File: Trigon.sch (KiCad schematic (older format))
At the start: 1 part

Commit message: Fully laid out board
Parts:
- removed U?: ProMicro, symbol keebio:ProMicro
- added D1, D10, D11, D12, D13, D14, D15, D16, D17, D18, D19, D2, D20, D21, D22, D23, D24, D25, D3, D4, D5, D6, D7, D8, D9: D_Small, Keebio-Parts:Diode, symbol Device:D_Small
- added MX1, MX10, MX11, MX12, MX13, MX14, MX15, MX16, MX17, MX18, MX19, MX2, MX20, MX21, MX22, MX23, MX24, MX25, MX3, MX4, MX5, MX6, MX7, MX8, MX9: MX-NoLED, MX_Alps_Hybrid:MX-1U-NoLED, symbol MX_Alps_Hybrid:MX-NoLED
- added U1: ProMicro, Keebio-Parts:ArduinoProMicro-ZigZag, symbol keebio:ProMicro
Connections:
- new net: D1.2 (A), MX1.2 (ROW)
- new net: D2.2 (A), MX2.2 (ROW)
- new net: D3.2 (A), MX3.2 (ROW)
- new net: D4.2 (A), MX4.2 (ROW)
- new net: D5.2 (A), MX5.2 (ROW)
- new net: D6.2 (A), MX6.2 (ROW)
- new net: D7.2 (A), MX7.2 (ROW)
- new net: D8.2 (A), MX8.2 (ROW)
- new net: D9.2 (A), MX9.2 (ROW)
- new net: D10.2 (A), MX10.2 (ROW)
- new net: D11.2 (A), MX11.2 (ROW)
- new net: D12.2 (A), MX12.2 (ROW)
- new net: D13.2 (A), MX13.2 (ROW)
- new net: D14.2 (A), MX14.2 (ROW)
- new net: D15.2 (A), MX15.2 (ROW)
- new net: D16.2 (A), MX16.2 (ROW)
- new net: D17.2 (A), MX17.2 (ROW)
- new net: D18.2 (A), MX18.2 (ROW)
- new net: D19.2 (A), MX19.2 (ROW)
- new net: D20.2 (A), MX20.2 (ROW)
- new net: D21.2 (A), MX21.2 (ROW)
- new net: D22.2 (A), MX22.2 (ROW)
- new net: D23.2 (A), MX23.2 (ROW)
- new net: D24.2 (A), MX24.2 (ROW)
- new net: D25.2 (A), MX25.2 (ROW)
- new net COL0: MX1.1 (COL), MX14.1 (COL), MX19.1 (COL), MX23.1 (COL), MX8.1 (COL), U1.8 (5/PC6)
- new net COL1: MX15.1 (COL), MX2.1 (COL), MX20.1 (COL), MX24.1 (COL), MX9.1 (COL), U1.7 (4/PD4)
- new net COL2: MX10.1 (COL), MX16.1 (COL), MX21.1 (COL), MX25.1 (COL), MX3.1 (COL), U1.6 (3/PD0)
- new net COL3: MX11.1 (COL), MX17.1 (COL), MX22.1 (COL), MX4.1 (COL), U1.5 (2/PD1)
- new net COL4: MX12.1 (COL), MX18.1 (COL), MX5.1 (COL), U1.9 (6/PD7)
- new net COL5: MX13.1 (COL), MX6.1 (COL), U1.10 (7/PE6)
- new net COL6: MX7.1 (COL), U1.11 (8/PB4)
- new net ROW0: D1.1 (K), D2.1 (K), D3.1 (K), D4.1 (K), D5.1 (K), D6.1 (K), D7.1 (K), U1.16 (15/PB1)
- new net ROW1: D10.1 (K), D11.1 (K), D12.1 (K), D13.1 (K), D8.1 (K), D9.1 (K), U1.17 (A0/PF7)
- new net ROW2: D14.1 (K), D15.1 (K), D16.1 (K), D17.1 (K), D18.1 (K), U1.18 (A1/PF6)
- new net ROW3: D19.1 (K), D20.1 (K), D21.1 (K), D22.1 (K), U1.19 (A2/PF5)
- new net ROW4: D23.1 (K), D24.1 (K), D25.1 (K), U1.20 (A3/PF4)

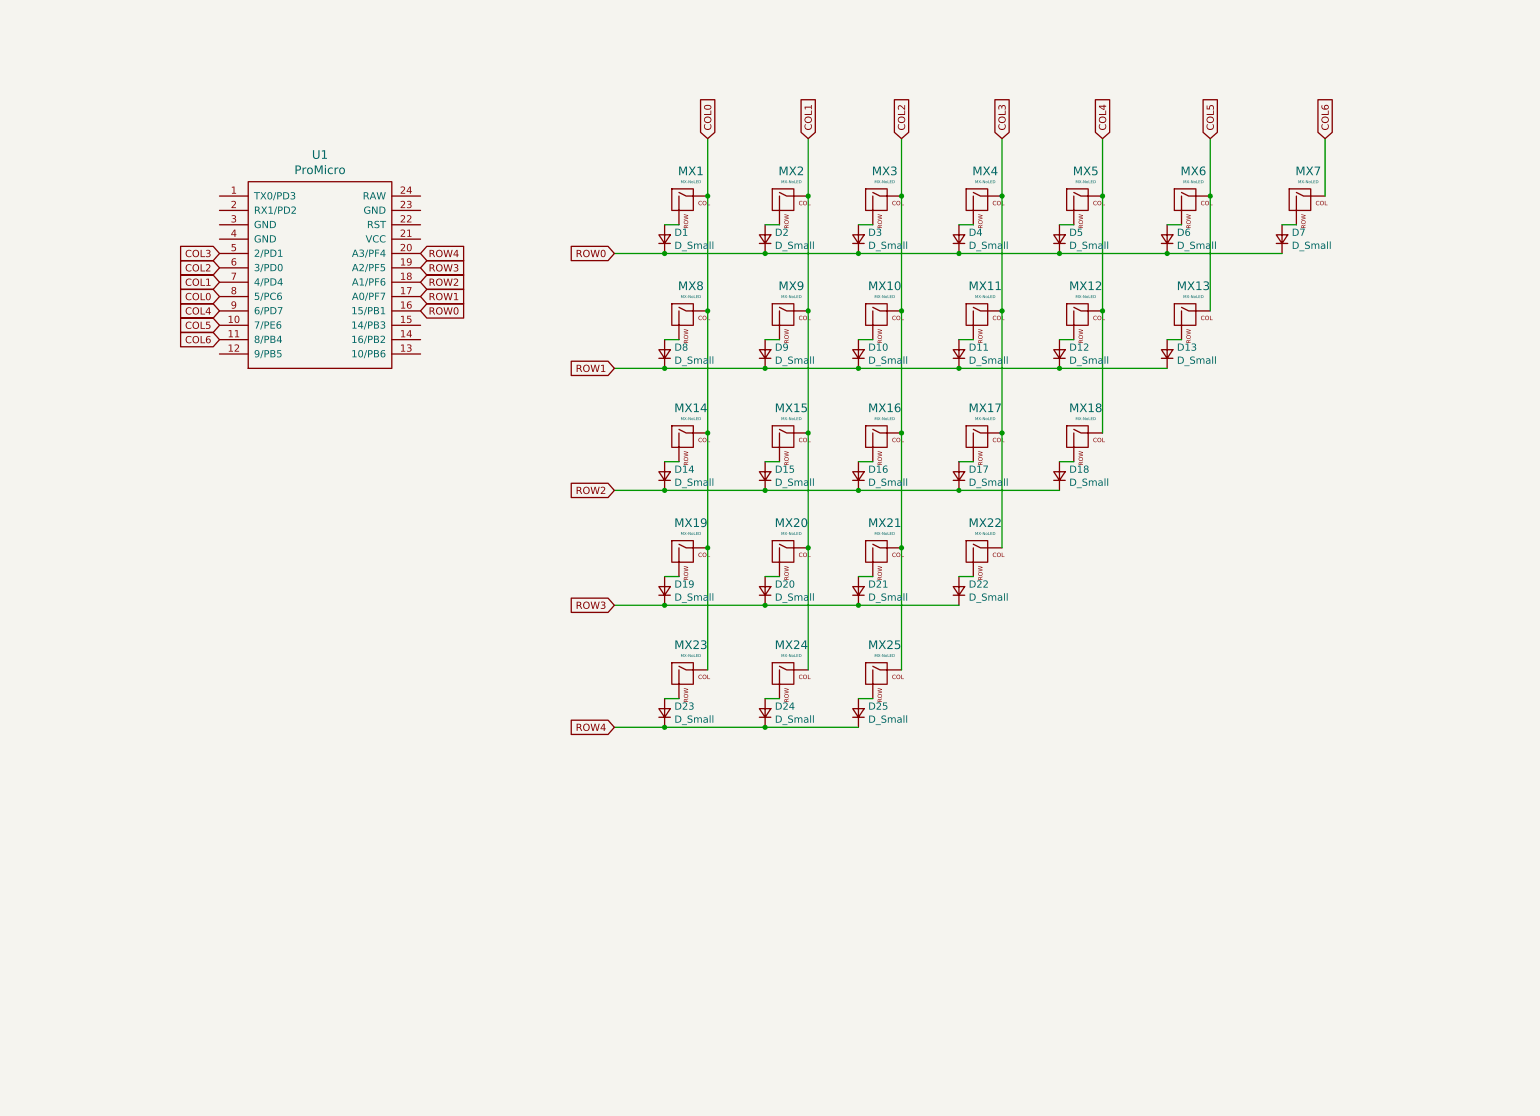
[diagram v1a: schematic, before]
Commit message: onboard usb c
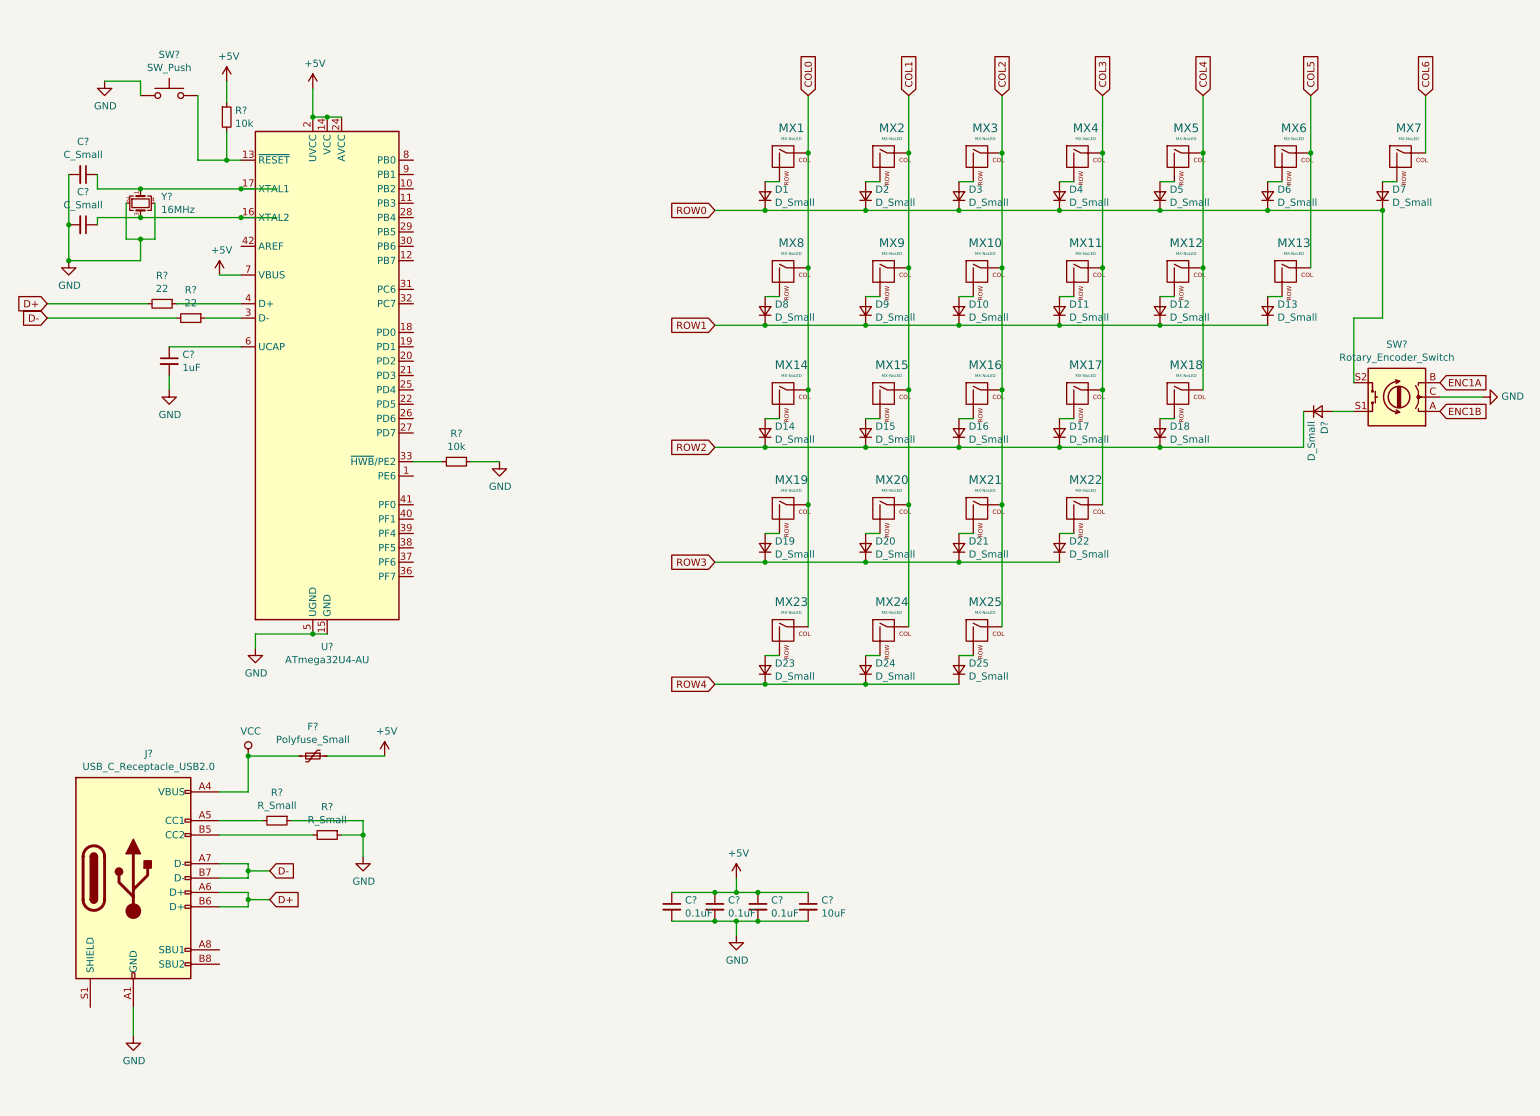
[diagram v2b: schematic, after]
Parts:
- removed U1: ProMicro, Keebio-Parts:ArduinoProMicro-ZigZag, symbol keebio:ProMicro
- added C?: 1uF, symbol Device:C_Small
- added C? (x3): 0.1uF, symbol Device:C_Small
- added C?: 10uF, symbol Device:C_Small
- added C? (x2): C_Small, symbol Device:C_Small
- added D?: D_Small, Keebio-Parts:Diode, symbol Device:D_Small
- added F?: Polyfuse_Small, symbol Device:Polyfuse_Small
- added J?: USB_C_Receptacle_USB2.0, symbol Connector:USB_C_Receptacle_USB2.0
- added R? (x2): 10k, symbol Device:R_Small
- added R? (x2): 22, symbol Device:R_Small
- added R? (x2): R_Small, symbol Device:R_Small
- added SW?: Rotary_Encoder_Switch, symbol Device:Rotary_Encoder_Switch
- added SW?: SW_Push, symbol Switch:SW_Push
- added U?: ATmega32U4-AU, Package_QFP:TQFP-44_10x10mm_P0.8mm, symbol MCU_Microchip_ATmega:ATmega32U4-AU
- added Y?: 16MHz, symbol Device:Crystal_GND24_Small
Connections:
- net ROW0: now also SW?.S2
- net ROW2: now also D?.1 (K)
- new net: R?.2, SW?.2, U?.13 (~RESET)
- new net: C?.1, U?.16 (XTAL2), Y?.3
- new net: C?.1, U?.17 (XTAL1), Y?.1
- new net: R?.1, U?.3 (D-)
- new net: R?.2, U?.33 (~HWB~/PE2)
- new net: R?.1, U?.4 (D+)
- new net: C?.1, U?.6 (UCAP)
- new net: D?.2 (A), SW?.S1
- new net: J?.A5 (CC1), R?.2
- new net: J?.B5 (CC2), R?.2
- new net +5V: C?.1, C?.1, C?.1, C?.1, F?.1, R?.1, U?.14 (VCC), U?.2 (UVCC), U?.24 (AVCC), U?.34 (VCC), U?.44 (AVCC), U?.7 (VBUS)
- new net D+: J?.A6 (D+), J?.B6 (D+), R?.2
- new net D-: J?.A7 (D-), J?.B7 (D-), R?.2
- new net ENC1A: SW?.B
- new net ENC1B: SW?.A
- new net GND: C?.2, C?.2, C?.2, C?.2, C?.2, C?.2, C?.2, J?.A1 (GND), J?.A12 (GND), J?.B1 (GND), J?.B12 (GND), R?.1, R?.1, R?.1, SW?.1, SW?.C, U?.15 (GND), U?.23 (GND), U?.35 (GND), U?.43 (GND), U?.5 (UGND), Y?.2, Y?.4
- new net VCC: F?.2, J?.A4 (VBUS), J?.A9 (VBUS), J?.B4 (VBUS), J?.B9 (VBUS)
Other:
- moved on the sheet: D1, D10, D11, D12, D13, D14, D15, D16, D17, D18, D19, D2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

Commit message: routed without rows cols
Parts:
- C1, C2: renamed from C?; value C_Small -> 22pF; footprint (none) -> Capacitor_SMD:C_0805_2012Metric
- C3, C4, C5, C6: renamed from C?; footprint (none) -> Capacitor_SMD:C_0805_2012Metric
- C7: renamed from C?; footprint (none) -> Diode_SMD:D_SOD-123
- D1, D10, D11, D12, D13, D14, D15, D16, D17, D18, D19, D2, D20, D21, D22, D23, D24, D25, D3, D4, D5, D6, D7, D8, D9: footprint Keebio-Parts:Diode -> Diode_SMD:D_SOD-123
- D26: renamed from D?; footprint Keebio-Parts:Diode -> Diode_SMD:D_SOD-123
- F1: renamed from F?; footprint (none) -> Fuse:Fuse_1206_3216Metric
- J1: renamed from J?; footprint (none) -> Connector_USB:USB_C_Receptacle_Palconn_UTC16-G
- MX1, MX10, MX11, MX12, MX13, MX14, MX15, MX16, MX17, MX18, MX19, MX2, MX20, MX21, MX22, MX23, MX24, MX25, MX3, MX4, MX5, MX6, MX7, MX8, MX9: footprint MX_Alps_Hybrid:MX-1U-NoLED -> MX_Only:MXOnly-1U-NoLED
- R1, R2, R3, R4, R5, R6: renamed from R?; footprint (none) -> Resistor_SMD:R_0805_2012Metric
- SW1: renamed from SW?; footprint (none) -> random-keyboard-parts:SKQG-1155865
- SW2: renamed from SW?; footprint (none) -> Rotary_Encoder:RotaryEncoder_Alps_EC12E-Switch_Vertical_H20mm
- Y1: renamed from Y?; footprint (none) -> Crystal:Crystal_SMD_3225-4Pin_3.2x2.5mm
- gave numbers to parts that had none: 1
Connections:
- net COL5: now also SW2.S2
- net GND: now also J1.S1 (SHIELD)
- net ROW0: no longer SW2.S2

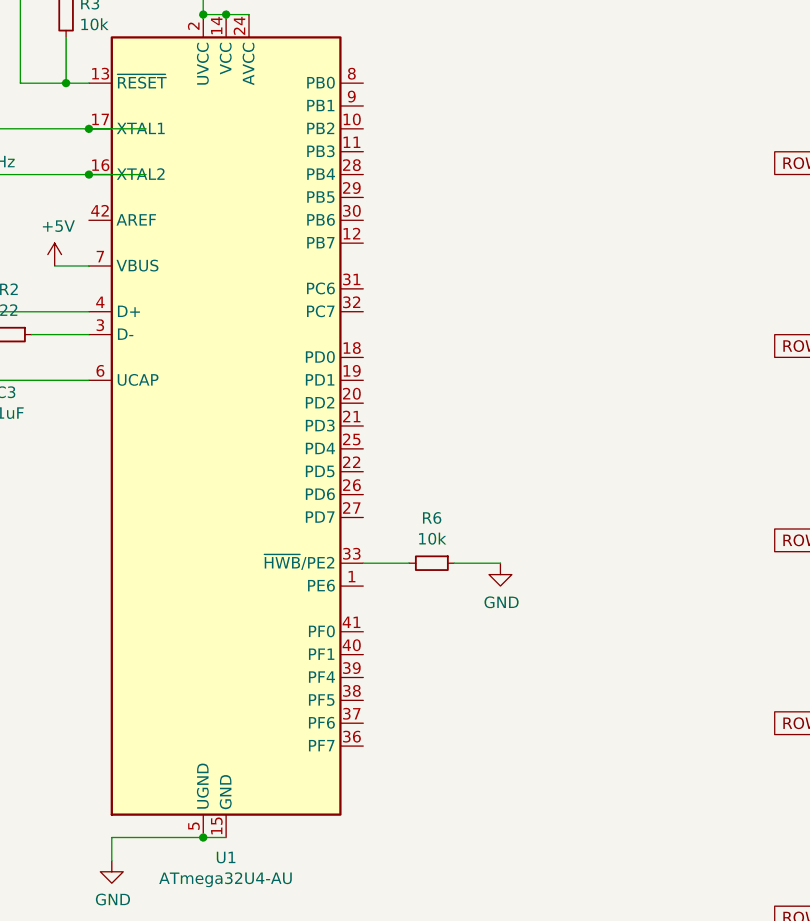
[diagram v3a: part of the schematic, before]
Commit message: fully routed matrix
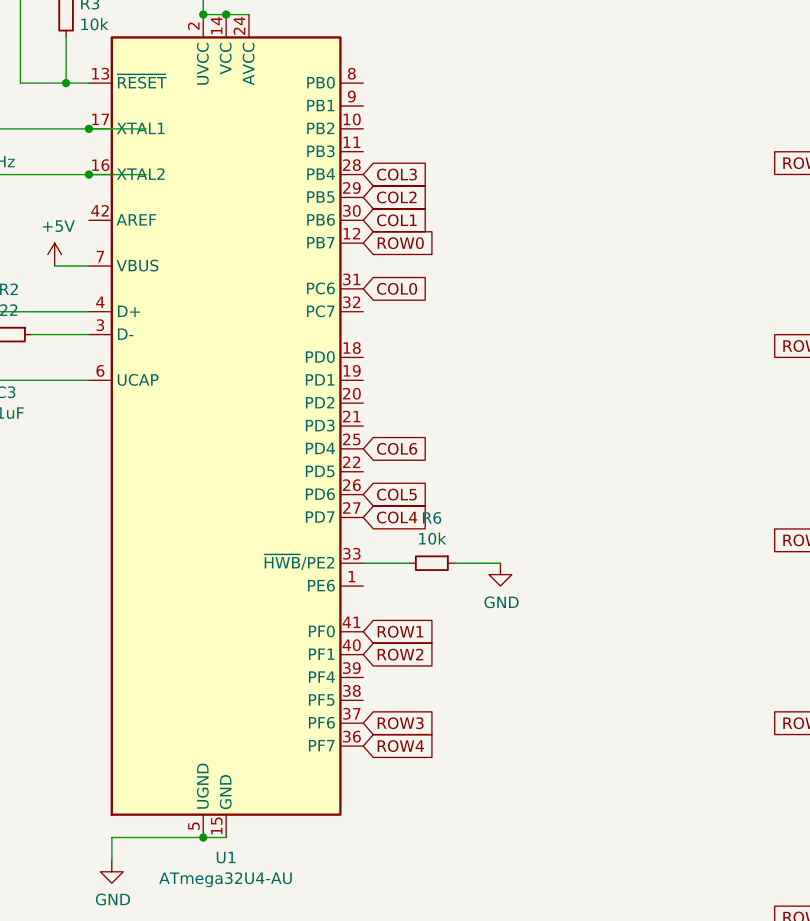
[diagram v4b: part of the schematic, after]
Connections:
- net COL0: now also U1.31 (PC6)
- net COL1: now also U1.30 (PB6)
- net COL2: now also U1.29 (PB5)
- net COL3: now also U1.28 (PB4)
- net COL4: now also U1.27 (PD7)
- net COL5: now also U1.26 (PD6)
- net COL6: now also U1.25 (PD4)
- net ROW0: now also U1.12 (PB7)
- net ROW1: now also U1.41 (PF0)
- net ROW2: now also U1.40 (PF1)
- net ROW3: now also U1.37 (PF6)
- net ROW4: now also U1.36 (PF7)
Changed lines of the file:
@@
 	9500 2950 9500 2150
 Connection ~ 9500 2150
+Text GLabel 3250 2300 2    50   Input ~ 0
+COL0
+Text GLabel 3250 2000 2    50   Input ~ 0
+COL1
+Text GLabel 3250 1900 2    50   Input ~ 0
+COL2
+Text GLabel 3250 1800 2    50   Input ~ 0
+COL3
+Text GLabel 3250 3300 2    50   Input ~ 0
+COL4
+Text GLabel 3250 3200 2    50   Input ~ 0
+COL5
+Text GLabel 3250 3000 2    50   Input ~ 0
+COL6
+Text GLabel 3250 2100 2    50   Input ~ 0
+ROW0
+Text GLabel 3250 4300 2    50   Input ~ 0
+ROW4
+Text GLabel 3250 4200 2    50   Input ~ 0
+ROW3
+Text GLabel 3250 3900 2    50   Input ~ 0
+ROW2
+Text GLabel 3250 3800 2    50   Input ~ 0
+ROW1
 $EndSCHEMATC

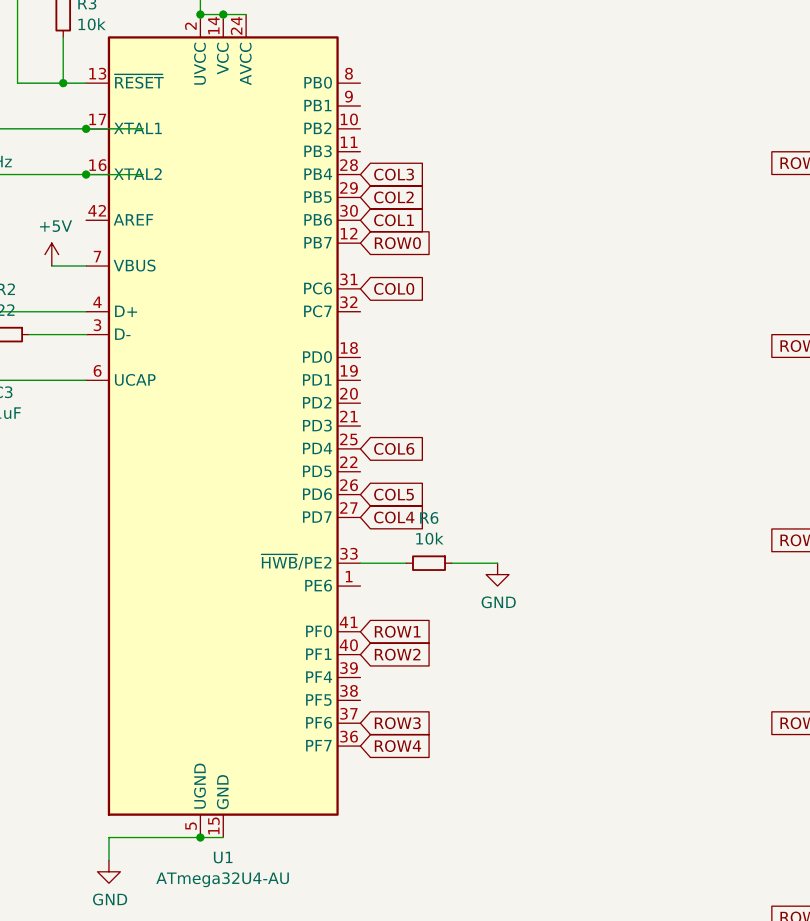
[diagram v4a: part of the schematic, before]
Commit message: all on one side
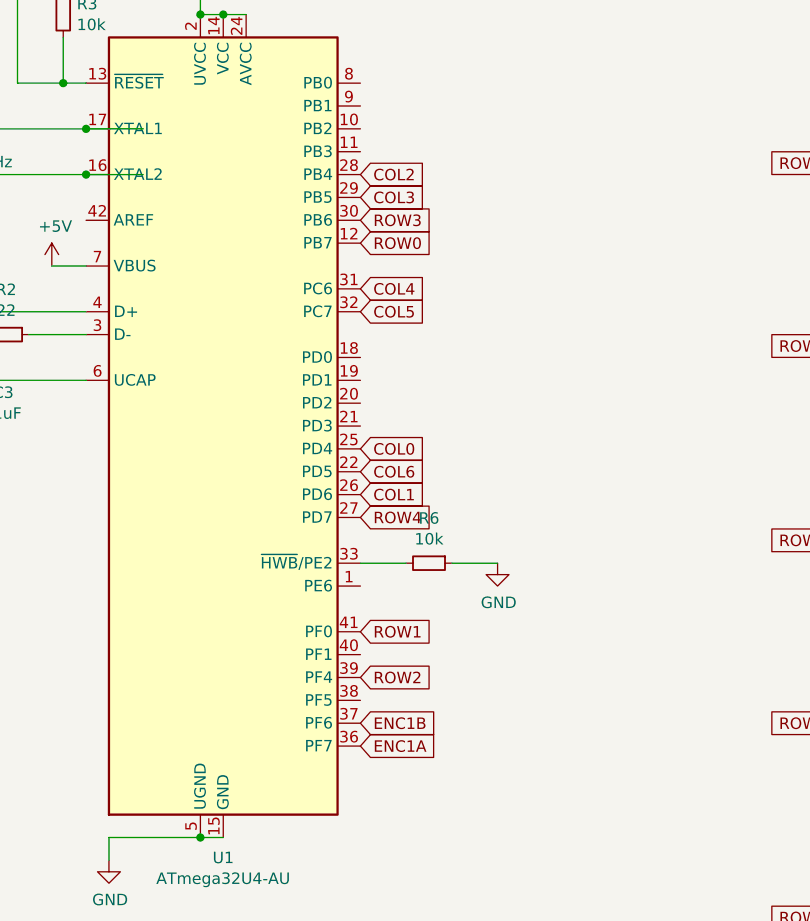
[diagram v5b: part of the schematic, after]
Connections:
- net COL0: now also U1.25 (PD4); no longer U1.31 (PC6)
- net COL1: now also U1.26 (PD6); no longer U1.30 (PB6)
- net COL2: now also U1.28 (PB4); no longer U1.29 (PB5)
- net COL3: now also U1.29 (PB5); no longer U1.28 (PB4)
- net COL4: now also U1.31 (PC6); no longer U1.27 (PD7)
- net COL5: now also U1.32 (PC7); no longer U1.26 (PD6)
- net COL6: now also U1.22 (PD5); no longer U1.25 (PD4)
- net ENC1A: now also U1.36 (PF7)
- net ENC1B: now also U1.37 (PF6)
- net ROW2: now also U1.39 (PF4); no longer U1.40 (PF1)
- net ROW3: now also U1.30 (PB6); no longer U1.37 (PF6)
- net ROW4: now also U1.27 (PD7); no longer U1.36 (PF7)
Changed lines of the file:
@@
 	9500 2950 9500 2150
 Connection ~ 9500 2150
+Text GLabel 3250 3000 2    50   Input ~ 0
+COL0
+Text GLabel 3250 3200 2    50   Input ~ 0
+COL1
+Text GLabel 3250 1800 2    50   Input ~ 0
+COL2
+Text GLabel 3250 1900 2    50   Input ~ 0
+COL3
 Text GLabel 3250 2300 2    50   Input ~ 0
-COL0
-Text GLabel 3250 2000 2    50   Input ~ 0
-COL1
-Text GLabel 3250 1900 2    50   Input ~ 0
-COL2
-Text GLabel 3250 1800 2    50   Input ~ 0
-COL3
-Text GLabel 3250 3300 2    50   Input ~ 0
 COL4
-Text GLabel 3250 3200 2    50   Input ~ 0
+Text GLabel 3250 2400 2    50   Input ~ 0
 COL5
-Text GLabel 3250 3000 2    50   Input ~ 0
+Text GLabel 3250 3100 2    50   Input ~ 0
 COL6
 Text GLabel 3250 2100 2    50   Input ~ 0
 ROW0
-Text GLabel 3250 4300 2    50   Input ~ 0
+Text GLabel 3250 3300 2    50   Input ~ 0
 ROW4
-Text GLabel 3250 4200 2    50   Input ~ 0
+Text GLabel 3250 2000 2    50   Input ~ 0
 ROW3
-Text GLabel 3250 3900 2    50   Input ~ 0
+Text GLabel 3250 4000 2    50   Input ~ 0
 ROW2
 Text GLabel 3250 3800 2    50   Input ~ 0
 ROW1
+Text GLabel 3250 4200 2    50   Input ~ 0
+ENC1B
+Text GLabel 3250 4300 2    50   Input ~ 0
+ENC1A
 $EndSCHEMATC
